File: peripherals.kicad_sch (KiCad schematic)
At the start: 92 parts, among them J10 533980471, J11 ERF8-040-05.0-L-DV-K-TR, J14 SM04B-SRSS-TB-LF-SN, J9 FTSH-105-01-F-DV-K, Q10 PJE138K, Q9 PJE138K, U30 TPD4E05U06QDQARQ1, U33 NTS0102GT, U34 PCAL6408ABSHP, U35 AP22653FDZ-7

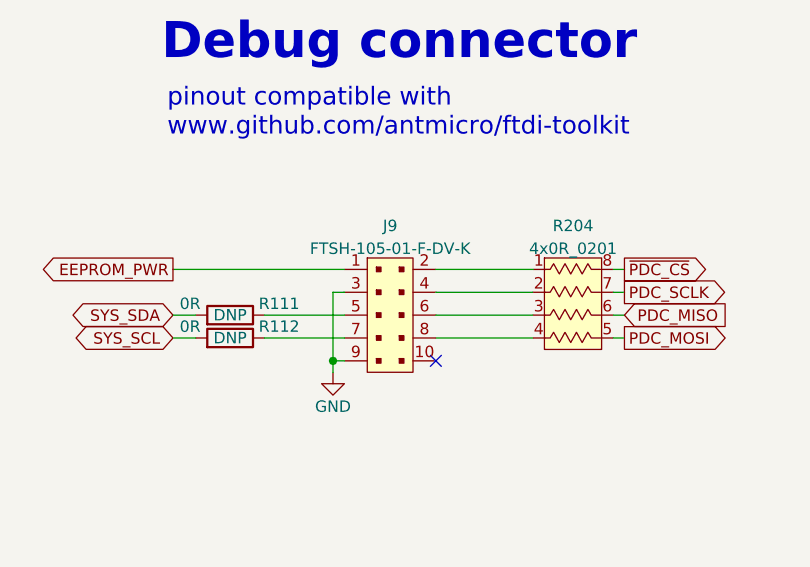
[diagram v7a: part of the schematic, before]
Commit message: Restore tag-connect, remove 2x5 1.27 header
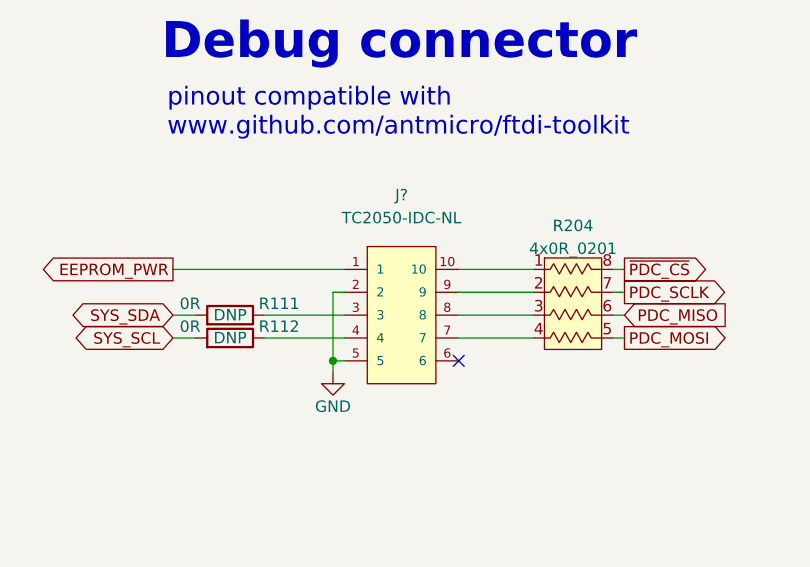
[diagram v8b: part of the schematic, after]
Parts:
- removed J9: FTSH-105-01-F-DV-K, antmicro-footprints:PinHeader_2x5_P1.27_SMD, symbol antmicroRectangularConnectorsHeadersMalePins:FTSH-105-01-F-DV-K
- added J?: TC2050-IDC-NL, jetson-orin-baseboard-footprints:TC2050-IDC-NL_2x05_Vertical, symbol jetson-orin-baseboard:TC2050-IDC-NL
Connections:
- net EEPROM_PWR: now also J?.1
- net GND: now also J?.2, J?.5
- net at R111.1: now also J?.3
- net at R112.1: now also J?.4
- net at R204.1: now also J?.10
- net at R204.2: now also J?.9
- net at R204.3: now also J?.8
- net at R204.4: now also J?.7
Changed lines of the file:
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@@
   (no_connect (at 189.23 199.39))
   (no_connect (at 189.23 196.85))
-  (no_connect (at 63.5 246.38))
   (no_connect (at 198.12 196.85))
   (no_connect (at 198.12 199.39))
   (no_connect (at 130.81 199.39))
+  (no_connect (at 66.04 246.38))
   (no_connect (at 130.81 158.75))
   (no_connect (at 130.81 161.29))
@@
     (stroke (width 0) (type default) (color 0 0 0 0))
   )
-  (wire (pts (xy 63.5 238.76) (xy 74.295 238.76))
-    (stroke (width 0) (type default) (color 0 0 0 0))
-  )
   (wire (pts (xy 209.55 263.525) (xy 209.55 264.795))
     (stroke (width 0) (type default) (color 0 0 0 0))
@@
     (stroke (width 0) (type default) (color 0 0 0 0))
   )
+  (wire (pts (xy 66.04 241.3) (xy 74.295 241.3))
+    (stroke (width 0) (type default) (color 0 0 0 0))
+  )
   (wire (pts (xy 328.93 245.11) (xy 330.2 245.11))
     (stroke (width 0) (type default) (color 0 0 0 0))
@@
     (stroke (width 0) (type default) (color 0 0 0 0))
   )
-  (wire (pts (xy 63.5 241.3) (xy 74.295 241.3))
-    (stroke (width 0) (type default) (color 0 0 0 0))
-  )
   (wire (pts (xy 196.85 93.98) (xy 182.88 93.98))
     (stroke (width 0) (type default) (color 0 0 0 0))
@@
     (stroke (width 0) (type default) (color 0 0 0 0))
   )
-  (wire (pts (xy 63.5 243.84) (xy 74.295 243.84))
-    (stroke (width 0) (type default) (color 0 0 0 0))
-  )
   (polyline (pts (xy 231.14 12.7) (xy 231.14 118.11))
     (stroke (width 0) (type default) (color 0 0 0 0))
@@
     (stroke (width 0) (type default) (color 0 0 0 0))
   )
+  (wire (pts (xy 66.04 238.76) (xy 74.295 238.76))
+    (stroke (width 0) (type default) (color 0 0 0 0))
+  )
   (wire (pts (xy 260.35 72.39) (xy 269.24 72.39))
     (stroke (width 0) (type default) (color 0 0 0 0))
@@
     (stroke (width 0) (type default) (color 0 0 0 0))
   )
+  (wire (pts (xy 66.04 236.22) (xy 74.295 236.22))
+    (stroke (width 0) (type default) (color 0 0 0 0))
+  )
   (wire (pts (xy 265.43 62.23) (xy 260.35 62.23))
     (stroke (width 0) (type default) (color 0 0 0 0))
@@
     (stroke (width 0) (type default) (color 0 0 0 0))
   )
-  (wire (pts (xy 63.5 236.22) (xy 74.295 236.22))
-    (stroke (width 0) (type default) (color 0 0 0 0))
-  )
   (wire (pts (xy 179.07 265.43) (xy 179.07 257.81))
     (stroke (width 0) (type default) (color 0 0 0 0))
@@
     (stroke (width 0) (type default) (color 0 0 0 0))
   )
+  (wire (pts (xy 66.04 243.84) (xy 74.295 243.84))
+    (stroke (width 0) (type default) (color 0 0 0 0))
+  )
   (wire (pts (xy 182.88 102.87) (xy 182.88 104.14))
     (stroke (width 0) (type default) (color 0 0 0 0))
@@
     (pin "2")
   )
+  (symbol (lib_id "jetson-orin-baseboard:TC2050-IDC-NL") (at 59.69 241.3 0) (unit 1)
+    (in_bom yes) (on_board yes) (fields_autoplaced)
+    (property "Reference" "J?" (id 0) (at 59.69 227.965 0))
+    (property "Value" "TC2050-IDC-NL" (id 1) (at 59.69 230.505 0))
+    (property "Footprint" "jetson-orin-baseboard-footprints:TC2050-IDC-NL_2x05_Vertical" (id 2) (at 53.34 241.3 0)
+      (effects (font (size 1.27 1.27)) (justify left bottom) hide)
+    )
+    (property "Datasheet" "" (id 3) (at 59.69 241.3 0)
+      (effects (font (size 1.27 1.27)) (justify left bottom) hide)
+    )
+    (property "MPN" "TC2050-IDC-NL" (id 4) (at 59.69 241.3 0)
+      (effects (font (size 1.27 1.27)) hide)
+    )
+    (property "Manufacturer" "Tag-Connect" (id 5) (at 59.69 241.3 0)
+      (effects (font (size 1.27 1.27)) hide)
+    )
+    (pin "1")
+    (pin "10")
+    (pin "2")
+    (pin "3")
+    (pin "4")
+    (pin "5")
+    (pin "6")
+    (pin "7")
+    (pin "8")
+    (pin "9")
+  )
   (symbol (lib_id "jetson-orin-baseboard:C_1u_0402") (at 367.03 172.72 0) (mirror y) (unit 1)
     (in_bom yes) (on_board yes) (fields_autoplaced)
@@
     (pin "2")
   )
-  (symbol (lib_id "antmicroRectangularConnectorsHeadersMalePins:FTSH-105-01-F-DV-K") (at 58.42 241.3 0) (unit 1)
-    (in_bom yes) (on_board yes) (fields_autoplaced)
-    (property "Reference" "J9" (id 0) (at 58.42 231.3772 0))
-    (property "Value" "FTSH-105-01-F-DV-K" (id 1) (at 58.42 233.9141 0))
-    (property "Footprint" "antmicro-footprints:PinHeader_2x5_P1.27_SMD" (id 2) (at 63.5 236.22 0)
-      (effects (font (size 1.27 1.27)) (justify left) hide)
-    )
-    (property "Datasheet" "http://suddendocs.samtec.com/prints/ftsh-1xx-xx-xxx-dv-xxx-xxx-mkt.pdf" (id 3) (at 63.5 233.68 0)
-      (effects (font (size 1.27 1.27)) (justify left) hide)
-    )
-    (property "MPN" "FTSH-105-01-F-DV-K" (id 4) (at 63.5 228.6 0)
-      (effects (font (size 1.524 1.524)) (justify left) hide)
-    )
-    (property "Manufacturer" "Samtec Inc." (id 5) (at 63.5 213.36 0)
-      (effects (font (size 1.524 1.524)) (justify left) hide)
-    )
-    (pin "1")
-    (pin "10")
-    (pin "2")
-    (pin "3")
-    (pin "4")
-    (pin "5")
-    (pin "6")
-    (pin "7")
-    (pin "8")
-    (pin "9")
-  )
   (symbol (lib_id "jetson-orin-baseboard:R_0R_0402") (at 52.07 86.36 90) (unit 1)
